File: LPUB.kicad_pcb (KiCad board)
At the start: 4 copper layers, 30 parts, among them IC1 ATMEGA324PA-AU, J1 Conn_01x06_Pin, J2 AVR-ISP-6, J3 Conn_02x10_Odd_Even, SW1 SW_MEC_5G, U1 LAMBDA80 (SX1280), U2 MB85RS64T, U4 LP2950-3.0_TO252, Y1 Crystal_GND24

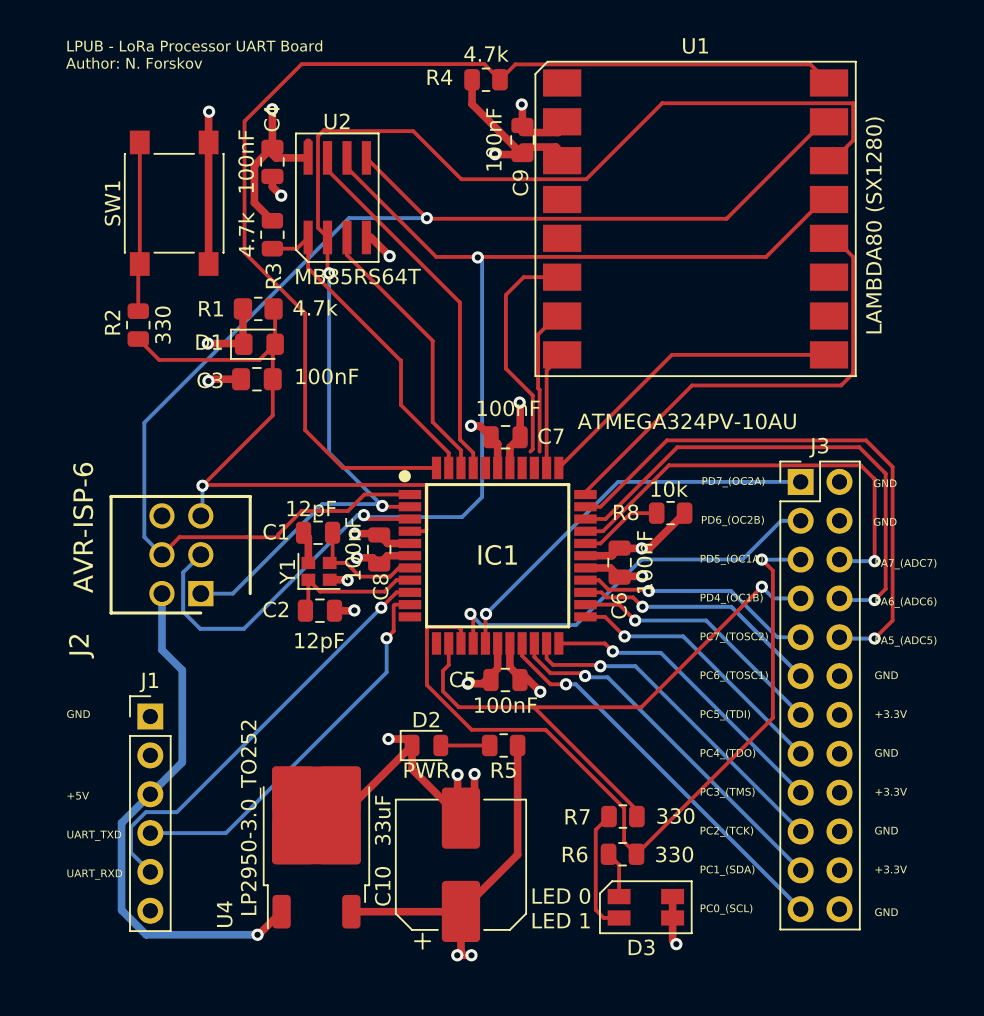
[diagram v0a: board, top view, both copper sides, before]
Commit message: added and connected Button A and B in PCB
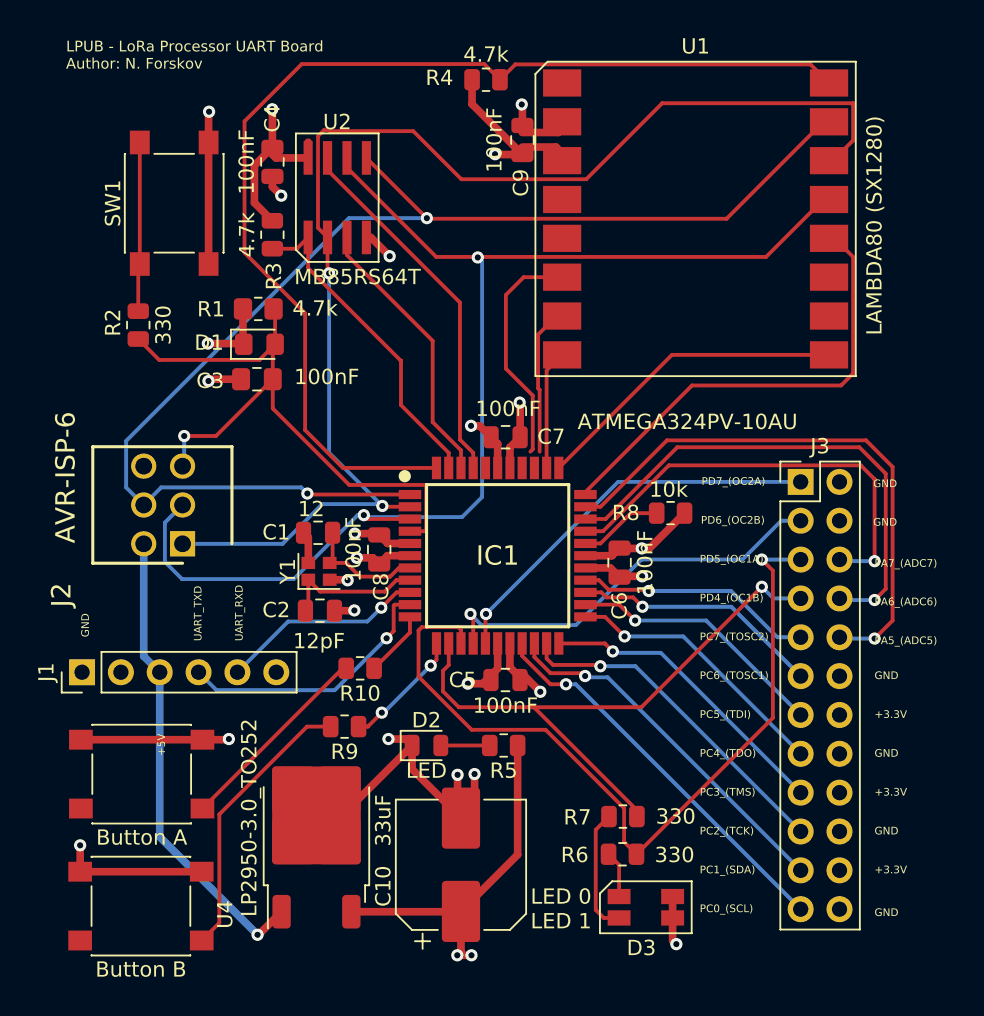
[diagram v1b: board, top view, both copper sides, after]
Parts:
- added R10: 1k, Resistor_SMD:R_0805_2012Metric, F.Cu at (108.6, 90.7)
- added R9: 1k, Resistor_SMD:R_0805_2012Metric, F.Cu at (107.6, 94.5)
- added SW2: Button A, DISCO_footprints:SW_Push_1P1T_NO_6x6mm_H9.5mm, F.Cu at (94.3, 97.6)
- added SW3: Button B, DISCO_footprints:SW_Push_1P1T_NO_6x6mm_H9.5mm, F.Cu at (94.3, 106.2)
- C1: value 12pF -> 12
- D2: value PWR -> LED
- SW1: value SW_MEC_5G -> Reset
- moved J1 5.32 mm to (90.4, 90.9), turned to 90 degrees
- moved J2 3.47 mm to (97.0, 82.5)
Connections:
- IC1 pad 11: unconnected-(IC1-(PCINT26/RXD1/INT0)_PD2-Pad11) -> Net-(IC1-(PCINT26/RXD1/INT0)_PD2)
- IC1 pad 12: unconnected-(IC1-(PCINT27/TXD1/INT1)_PD3-Pad12) -> Net-(IC1-(PCINT27/TXD1/INT1)_PD3)
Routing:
- net GND: track 70.0 -> 89.3 mm, vias 15 -> 17
- net Net-(SW3-A): track 0.00 -> 18.4 mm
- net /UART_RXD: track 28.1 -> 13.4 mm
- net Net-(SW2-A): track 0.00 -> 13.2 mm
- net Net-(IC1-(PCINT27/TXD1/INT1)_PD3): track 0.00 -> 7.98 mm, vias 0 -> 2
- net /UART_TXD: track 25.4 -> 17.6 mm
- net Net-(IC1-(PCINT26/RXD1/INT0)_PD2): track 0.00 -> 4.34 mm
- net +5V: track 35.3 -> 31.5 mm
- net /MOSI: track 85.6 -> 83.0 mm, vias 1 -> 2
- net /AVR_RESET: track 44.2 -> 42.1 mm
- net /PD5_(OC1A): track 52.3 -> 53.0 mm
